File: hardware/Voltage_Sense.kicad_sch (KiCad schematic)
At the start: 0 parts

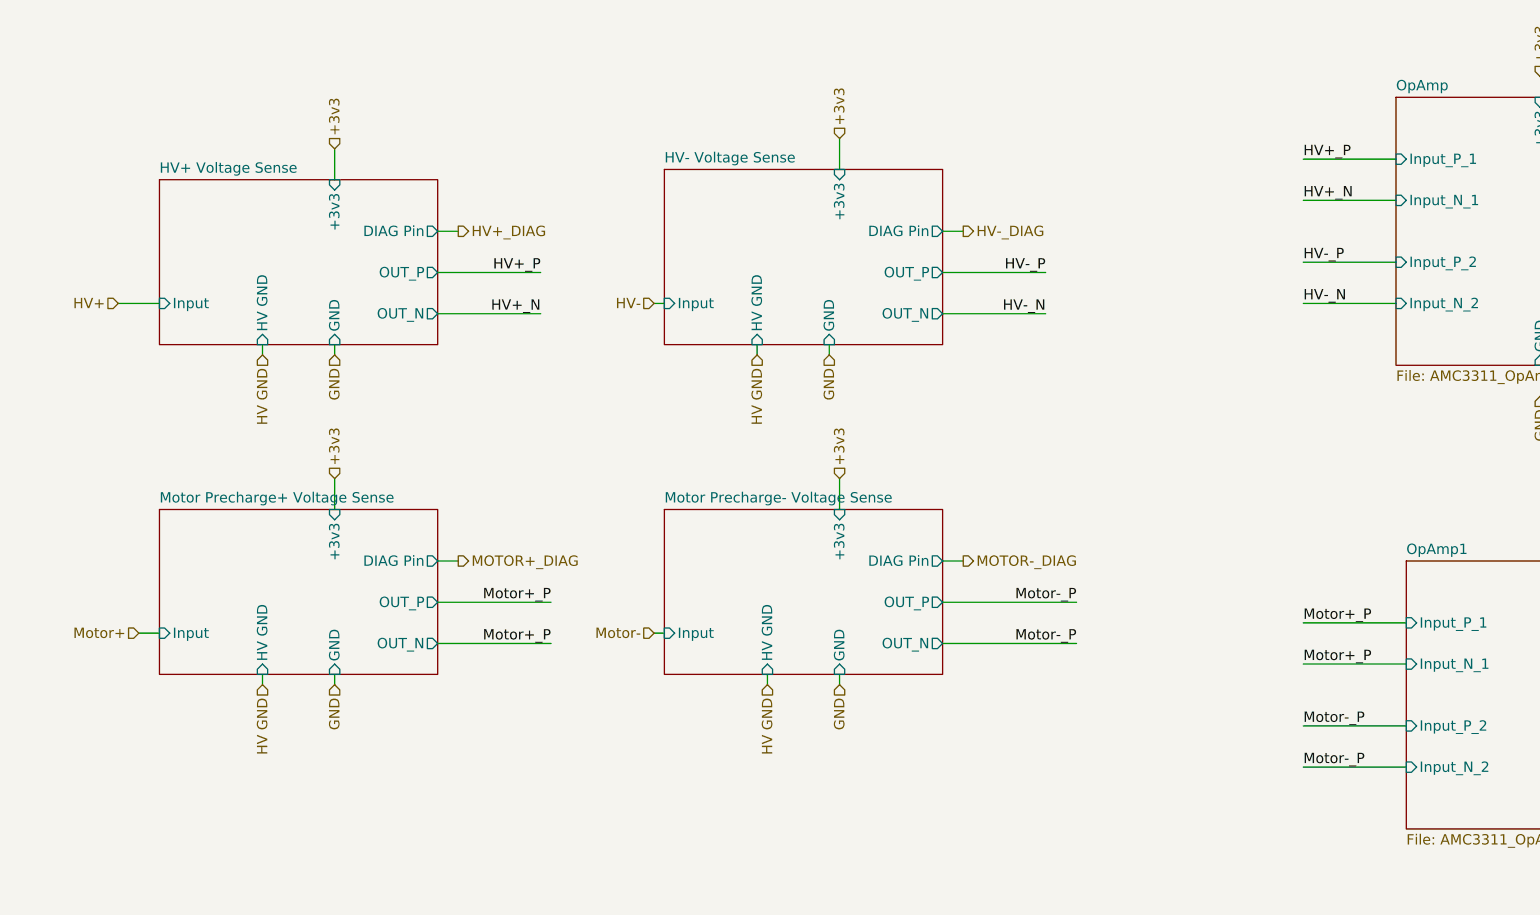
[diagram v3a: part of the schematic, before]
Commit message: added outside test points, removed unncessary symbol fields
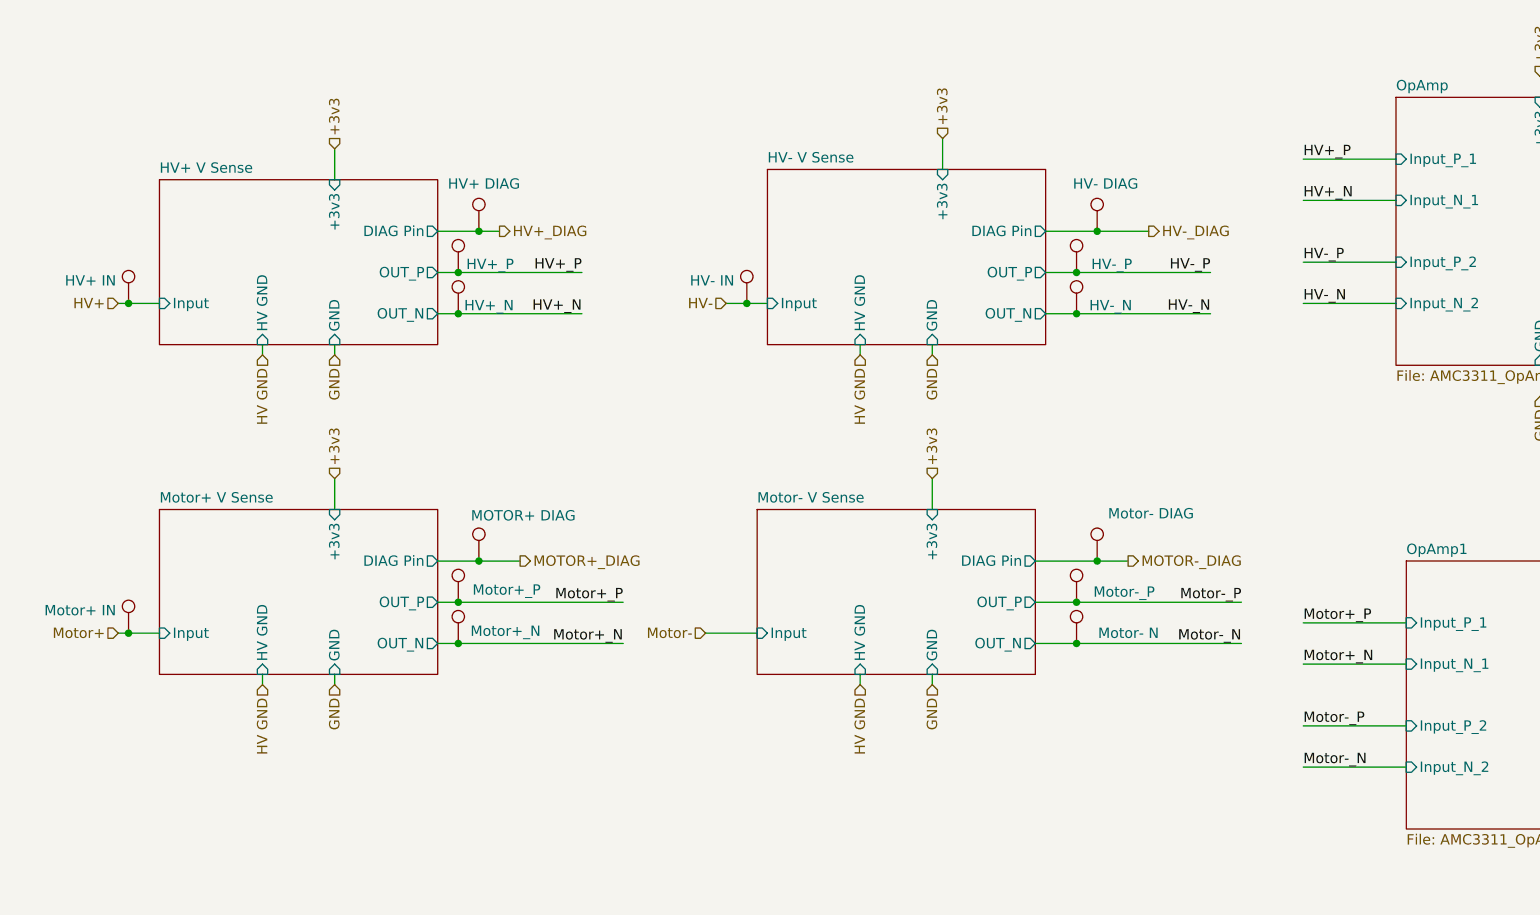
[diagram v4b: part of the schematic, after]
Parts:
- added TP?: Motor+ IN, TestPoint:TestPoint_THTPad_D3.0mm_Drill1.5mm, symbol Connector:TestPoint
- added TP?: HV- DIAG, TestPoint:TestPoint_THTPad_D3.0mm_Drill1.5mm, symbol Connector:TestPoint
- added TP?: Motor+_N, TestPoint:TestPoint_THTPad_D3.0mm_Drill1.5mm, symbol Connector:TestPoint
- added TP?: Motor+_P, TestPoint:TestPoint_THTPad_D3.0mm_Drill1.5mm, symbol Connector:TestPoint
- added TP?: Motor- N, TestPoint:TestPoint_THTPad_D3.0mm_Drill1.5mm, symbol Connector:TestPoint
- added TP?: Motor- DIAG, TestPoint:TestPoint_THTPad_D3.0mm_Drill1.5mm, symbol Connector:TestPoint
- added TP?: MOTOR+ DIAG, TestPoint:TestPoint_THTPad_D3.0mm_Drill1.5mm, symbol Connector:TestPoint
- added TP?: HV-_N, TestPoint:TestPoint_THTPad_D3.0mm_Drill1.5mm, symbol Connector:TestPoint
- added TP?: HV+ IN, TestPoint:TestPoint_THTPad_D3.0mm_Drill1.5mm, symbol Connector:TestPoint
- added TP?: HV- IN, TestPoint:TestPoint_THTPad_D3.0mm_Drill1.5mm, symbol Connector:TestPoint
- added TP?: HV+_P, TestPoint:TestPoint_THTPad_D3.0mm_Drill1.5mm, symbol Connector:TestPoint
- added TP?: HV+_N, TestPoint:TestPoint_THTPad_D3.0mm_Drill1.5mm, symbol Connector:TestPoint
- added TP?: HV-_P, TestPoint:TestPoint_THTPad_D3.0mm_Drill1.5mm, symbol Connector:TestPoint
- added TP?: HV+ DIAG, TestPoint:TestPoint_THTPad_D3.0mm_Drill1.5mm, symbol Connector:TestPoint
- added TP?: Motor-_P, TestPoint:TestPoint_THTPad_D3.0mm_Drill1.5mm, symbol Connector:TestPoint
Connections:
- net HV+: now also TP?.1
- net HV+_DIAG: now also TP?.1
- net HV+_N: now also TP?.1
- net HV+_P: now also TP?.1
- net HV-: now also TP?.1
- net HV-_DIAG: now also TP?.1
- net HV-_N: now also TP?.1
- net HV-_P: now also TP?.1
- net MOTOR+_DIAG: now also TP?.1
- net MOTOR-_DIAG: now also TP?.1
- net Motor+: now also TP?.1
- net Motor+_P: now also TP?.1
- net Motor-_P: now also TP?.1
- new net Motor+_N: TP?.1
- new net Motor-_N: TP?.1
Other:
- sheet HV+ Voltage Sense renamed HV+ V Sense
- sheet HV- Voltage Sense renamed HV- V Sense
- sheet Motor Precharge+ Voltage Sense renamed Motor+ V Sense
- sheet Motor Precharge- Voltage Sense renamed Motor- V Sense

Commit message: updated kicad sharepoint, added pn
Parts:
- gave numbers to parts that had none: 15
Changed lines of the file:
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@@
 		(in_pos_files yes)
 		(dnp no)
-		(property "Reference" "TP?"
+		(property "Reference" "TP20"
 			(at 31.75 100.8379 0)
 			(hide yes)
@@
 			(project "PS-HVCarrier"
 				(path "/2365a867-6254-4a7c-9718-f325e0bbac5c/83ab5b0b-4732-42c0-82fe-e74f4113c82a"
-					(reference "TP?")
+					(reference "TP20")
 					(unit 1)
 				)
@@
 		(in_pos_files yes)
 		(dnp no)
-		(property "Reference" "TP?"
+		(property "Reference" "TP32"
 			(at 151.13 51.3079 0)
 			(hide yes)
@@
 			(project "PS-HVCarrier"
 				(path "/2365a867-6254-4a7c-9718-f325e0bbac5c/83ab5b0b-4732-42c0-82fe-e74f4113c82a"
-					(reference "TP?")
+					(reference "TP32")
 					(unit 1)
 				)
@@
 		(in_pos_files yes)
 		(dnp no)
-		(property "Reference" "TP?"
+		(property "Reference" "TP24"
 			(at 72.39 102.1079 0)
 			(hide yes)
@@
 			(project "PS-HVCarrier"
 				(path "/2365a867-6254-4a7c-9718-f325e0bbac5c/83ab5b0b-4732-42c0-82fe-e74f4113c82a"
-					(reference "TP?")
+					(reference "TP24")
 					(unit 1)
 				)
@@
 		(in_pos_files yes)
 		(dnp no)
-		(property "Reference" "TP?"
+		(property "Reference" "TP23"
 			(at 72.39 97.0279 0)
 			(hide yes)
@@
 			(project "PS-HVCarrier"
 				(path "/2365a867-6254-4a7c-9718-f325e0bbac5c/83ab5b0b-4732-42c0-82fe-e74f4113c82a"
-					(reference "TP?")
+					(reference "TP23")
 					(unit 1)
 				)
@@
 		(in_pos_files yes)
 		(dnp no)
-		(property "Reference" "TP?"
+		(property "Reference" "TP31"
 			(at 148.59 102.1079 0)
 			(hide yes)
@@
 			(project "PS-HVCarrier"
 				(path "/2365a867-6254-4a7c-9718-f325e0bbac5c/83ab5b0b-4732-42c0-82fe-e74f4113c82a"
-					(reference "TP?")
+					(reference "TP31")
 					(unit 1)
 				)
@@
 		(in_pos_files yes)
 		(dnp no)
-		(property "Reference" "TP?"
+		(property "Reference" "TP33"
 			(at 151.13 91.9479 0)
 			(hide yes)
@@
 			(project "PS-HVCarrier"
 				(path "/2365a867-6254-4a7c-9718-f325e0bbac5c/83ab5b0b-4732-42c0-82fe-e74f4113c82a"
-					(reference "TP?")
+					(reference "TP33")
 					(unit 1)
 				)
@@
 		(in_pos_files yes)
 		(dnp no)
-		(property "Reference" "TP?"
+		(property "Reference" "TP26"
 			(at 74.93 91.9479 0)
 			(hide yes)
@@
 			(project "PS-HVCarrier"
 				(path "/2365a867-6254-4a7c-9718-f325e0bbac5c/83ab5b0b-4732-42c0-82fe-e74f4113c82a"
-					(reference "TP?")
+					(reference "TP26")
 					(unit 1)
 				)
@@
 		(in_pos_files yes)
 		(dnp no)
-		(property "Reference" "TP?"
+		(property "Reference" "TP29"
 			(at 148.59 61.4679 0)
 			(hide yes)
@@
 			(project "PS-HVCarrier"
 				(path "/2365a867-6254-4a7c-9718-f325e0bbac5c/83ab5b0b-4732-42c0-82fe-e74f4113c82a"
-					(reference "TP?")
+					(reference "TP29")
 					(unit 1)
 				)
@@
 		(in_pos_files yes)
 		(dnp no)
-		(property "Reference" "TP?"
+		(property "Reference" "TP19"
 			(at 31.75 60.1979 0)
 			(hide yes)
@@
 			(project "PS-HVCarrier"
 				(path "/2365a867-6254-4a7c-9718-f325e0bbac5c/83ab5b0b-4732-42c0-82fe-e74f4113c82a"
-					(reference "TP?")
+					(reference "TP19")
 					(unit 1)
 				)
@@
 		(in_pos_files yes)
 		(dnp no)
-		(property "Reference" "TP?"
+		(property "Reference" "TP27"
 			(at 107.95 60.1979 0)
 			(hide yes)
@@
 			(project "PS-HVCarrier"
 				(path "/2365a867-6254-4a7c-9718-f325e0bbac5c/83ab5b0b-4732-42c0-82fe-e74f4113c82a"
-					(reference "TP?")
+					(reference "TP27")
 					(unit 1)
 				)
@@
 		(in_pos_files yes)
 		(dnp no)
-		(property "Reference" "TP?"
+		(property "Reference" "TP21"
 			(at 72.39 56.3879 0)
 			(hide yes)
@@
 			(project "PS-HVCarrier"
 				(path "/2365a867-6254-4a7c-9718-f325e0bbac5c/83ab5b0b-4732-42c0-82fe-e74f4113c82a"
-					(reference "TP?")
+					(reference "TP21")
 					(unit 1)
 				)
@@
 		(in_pos_files yes)
 		(dnp no)
-		(property "Reference" "TP?"
+		(property "Reference" "TP22"
 			(at 72.39 61.4679 0)
 			(hide yes)
@@
 			(project "PS-HVCarrier"
 				(path "/2365a867-6254-4a7c-9718-f325e0bbac5c/83ab5b0b-4732-42c0-82fe-e74f4113c82a"
-					(reference "TP?")
+					(reference "TP22")
 					(unit 1)
 				)
@@
 		(in_pos_files yes)
 		(dnp no)
-		(property "Reference" "TP?"
+		(property "Reference" "TP28"
 			(at 148.59 56.3879 0)
 			(hide yes)
@@
 			(project "PS-HVCarrier"
 				(path "/2365a867-6254-4a7c-9718-f325e0bbac5c/83ab5b0b-4732-42c0-82fe-e74f4113c82a"
-					(reference "TP?")
+					(reference "TP28")
 					(unit 1)
 				)
@@
 		(in_pos_files yes)
 		(dnp no)
-		(property "Reference" "TP?"
+		(property "Reference" "TP25"
 			(at 74.93 51.3079 0)
 			(hide yes)
@@
 			(project "PS-HVCarrier"
 				(path "/2365a867-6254-4a7c-9718-f325e0bbac5c/83ab5b0b-4732-42c0-82fe-e74f4113c82a"
-					(reference "TP?")
+					(reference "TP25")
 					(unit 1)
 				)
@@
 		(in_pos_files yes)
 		(dnp no)
-		(property "Reference" "TP?"
+		(property "Reference" "TP30"
 			(at 148.59 97.0279 0)
 			(hide yes)
@@
 			(project "PS-HVCarrier"
 				(path "/2365a867-6254-4a7c-9718-f325e0bbac5c/83ab5b0b-4732-42c0-82fe-e74f4113c82a"
-					(reference "TP?")
-					(unit 1)
-				)
+					(reference "TP30")
+					(unit 1)
+				)
